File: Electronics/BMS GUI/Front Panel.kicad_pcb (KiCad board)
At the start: 2 copper layers, 44 x 50 mm, 24 parts, among them J101 OpenBMSRiser, J102 Programming, SW101 SW_Push, SW102 SW_Push, SW103 SW_Push, U101 MSP430G2755IDA38, U102 JLX12864G

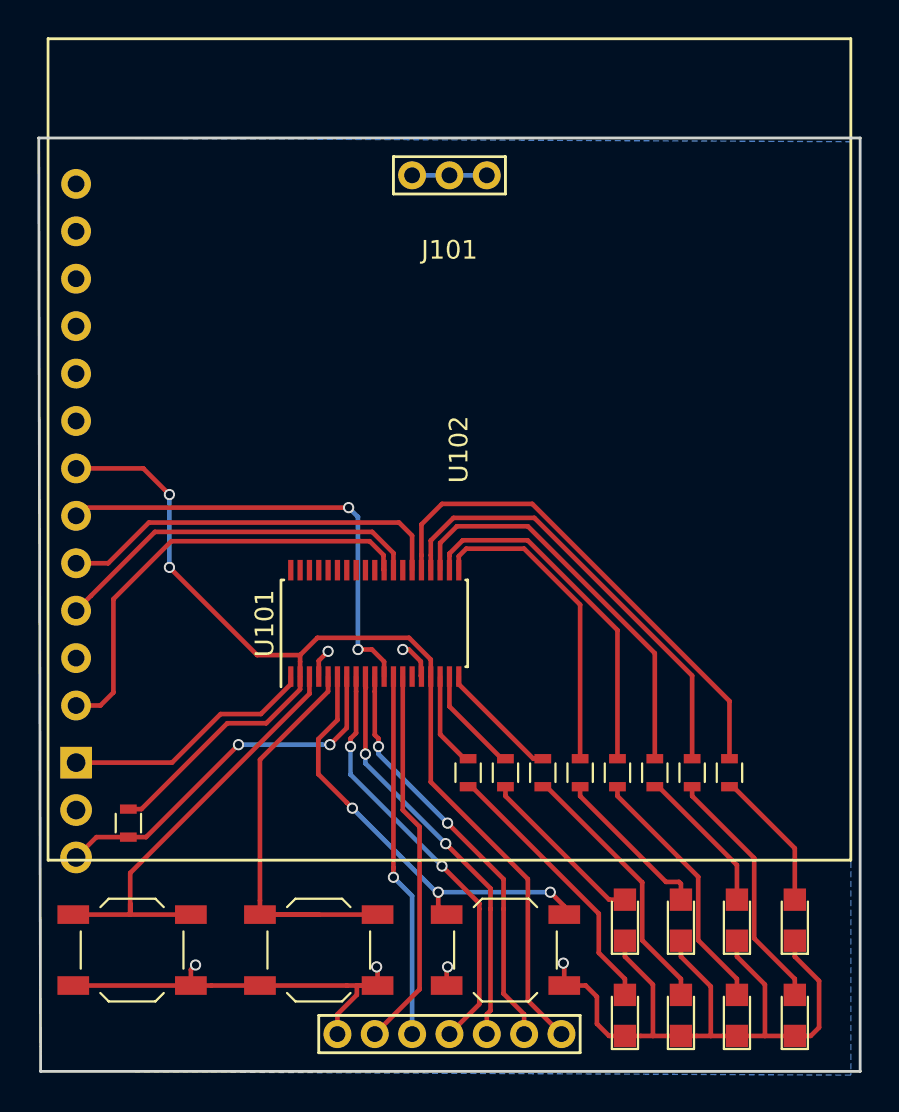
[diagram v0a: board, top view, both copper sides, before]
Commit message: Finish layout of front panel
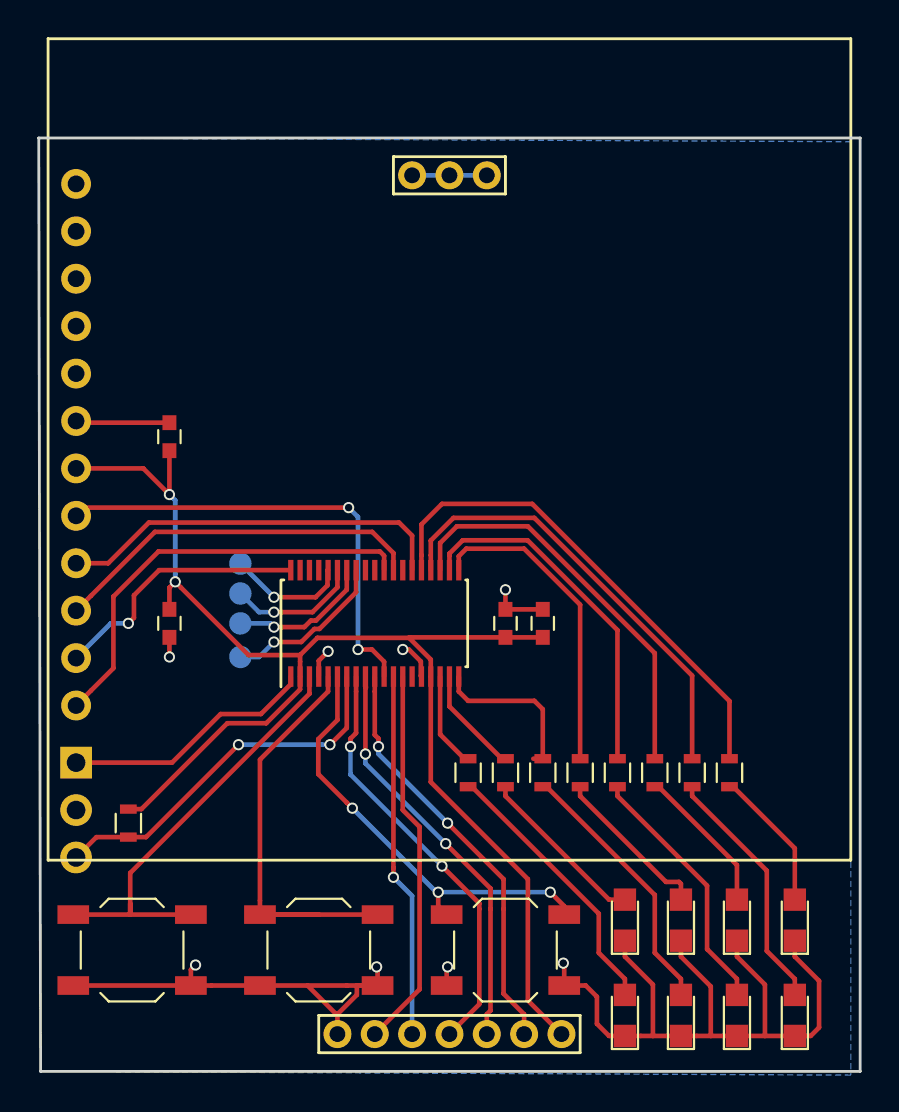
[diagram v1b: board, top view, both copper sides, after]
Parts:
- added C101: C, Capacitors_SMD:C_0603, F.Cu at (96.0, 102.0)
- added C102: C, Capacitors_SMD:C_0603, F.Cu at (114.0, 102.0)
- added C103: C, Capacitors_SMD:C_0603, F.Cu at (96.0, 92.0)
- added C104: C, Capacitors_SMD:C_0603, F.Cu at (116.0, 102.0)
- added J103: TEST_1P, conn-test:TEST-SMD-SMALL, B.Cu at (99.8, 103.8)
- added J104: TEST_1P, conn-test:TEST-SMD-SMALL, B.Cu at (99.8, 102.0)
- added J105: TEST_1P, conn-test:TEST-SMD-SMALL, B.Cu at (99.8, 100.4)
- added J106: TEST_1P, conn-test:TEST-SMD-SMALL, B.Cu at (99.8, 98.8)
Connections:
- U101 pad 31: (no net) -> Net-(J103-Pad1)
- U101 pad 32: (no net) -> Net-(J104-Pad1)
- U101 pad 33: (no net) -> Net-(J105-Pad1)
- U101 pad 34: (no net) -> Net-(J106-Pad1)
- U101 pad 38: (no net) -> /~LCD_RESET
- U102 pad 11: (no net) -> /~LCD_RESET
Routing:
- net /~LCD_RESET: track 0.00 -> 14.2 mm, vias 0 -> 1
- net VDD: track 62.9 -> 74.3 mm
- net GND: track 70.7 -> 82.1 mm, vias 6 -> 8
- net Net-(J103-Pad1): track 0.00 -> 8.82 mm, vias 0 -> 1
- net Net-(J104-Pad1): track 0.00 -> 7.66 mm, vias 0 -> 1
- net Net-(J105-Pad1): track 0.00 -> 7.08 mm, vias 0 -> 1
- net Net-(J106-Pad1): track 0.00 -> 6.52 mm, vias 0 -> 1
- net Net-(R106-Pad1): track 6.56 -> 9.26 mm
- net /CS: track 24.2 -> 23.0 mm
